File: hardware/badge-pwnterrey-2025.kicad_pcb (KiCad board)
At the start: 2 copper layers, 47 x 50 mm, 0 parts

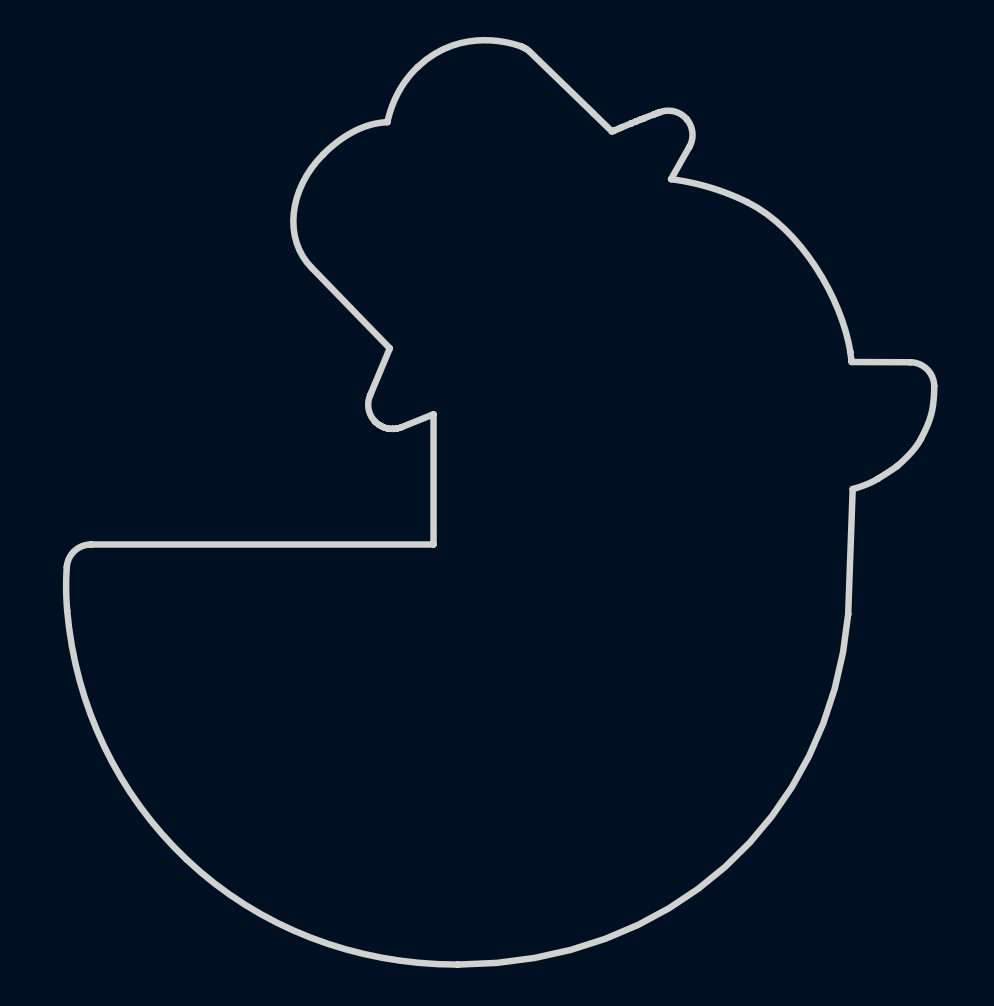
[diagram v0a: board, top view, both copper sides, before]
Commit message: feat(hw): add floorplan
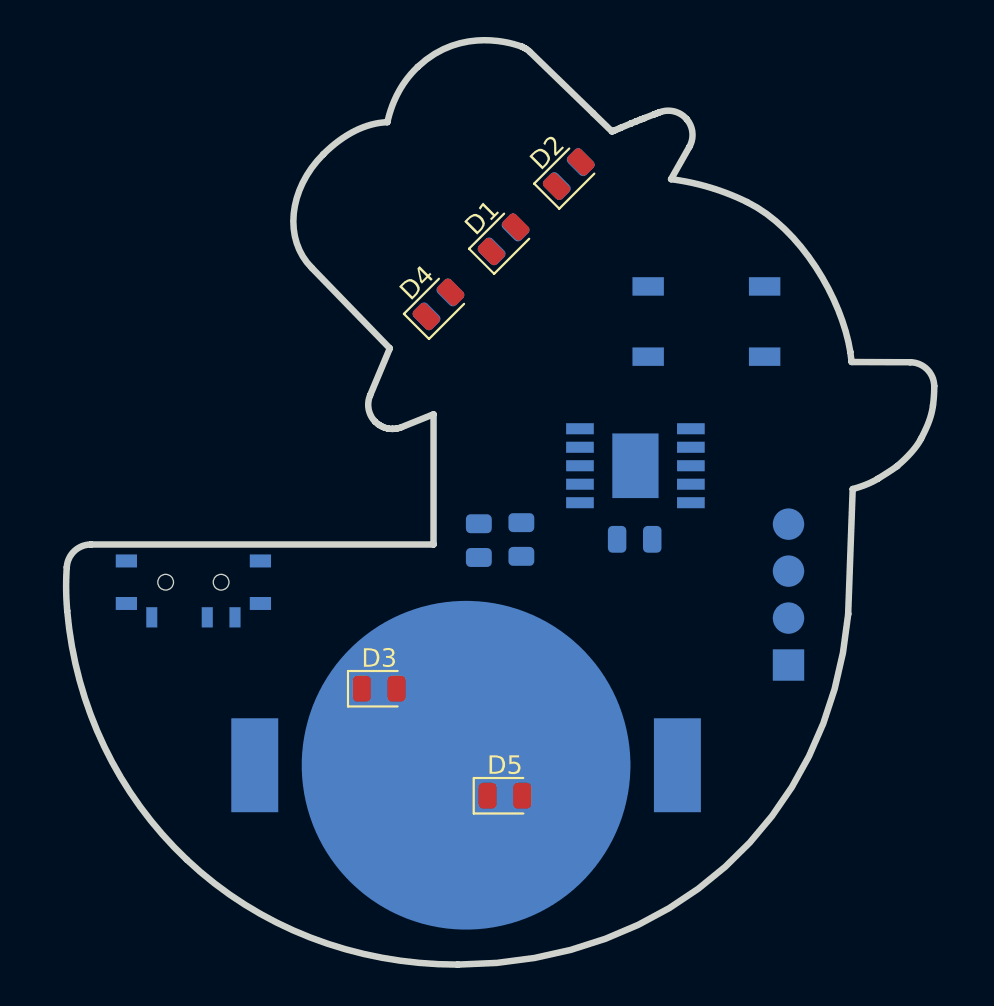
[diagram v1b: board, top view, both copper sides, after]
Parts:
- added BT1: Battery_Cell, Library:BAT-HLD-001, B.Cu at (145.0, 113.0)
- added C1: 0.1uF, Capacitor_SMD:C_0805_2012Metric, B.Cu at (154.1, 100.8)
- added D1: Orange, LED_SMD:LED_0805_2012Metric, F.Cu at (147.0, 84.5)
- added D2: Red, LED_SMD:LED_0805_2012Metric, F.Cu at (150.6, 81.0)
- added D3: Blue, LED_SMD:LED_0805_2012Metric, F.Cu at (140.3, 108.9)
- added D4: Green, LED_SMD:LED_0805_2012Metric, F.Cu at (143.5, 88.1)
- added D5: Yellow, LED_SMD:LED_0805_2012Metric, F.Cu at (147.1, 114.7)
- added J1: Conn_01x04_Socket, Connector_PinHeader_2.54mm:PinHeader_1x04_P2.54mm_Vertical, B.Cu at (162.4, 107.6)
- added R1: 330R, Resistor_SMD:R_0805_2012Metric, B.Cu at (147.0, 84.6)
- added R2: 330R, Resistor_SMD:R_0805_2012Metric, B.Cu at (150.6, 81.0)
- added R3: 330R, Resistor_SMD:R_0805_2012Metric, B.Cu at (145.7, 100.8)
- added R4: 330R, Resistor_SMD:R_0805_2012Metric, B.Cu at (143.5, 88.1)
- added R5: 330R, Resistor_SMD:R_0805_2012Metric, B.Cu at (148.0, 100.8)
- added SW1: SW_RST, Button_Switch_SMD:SW_SPST_TL3342, B.Cu at (158.0, 89.0)
- added SW2: On, Library:MSK12C02, B.Cu at (130.2, 103.1)
- added U1: PY32F002AA15M6TU, Library:PY32F002AA15M, B.Cu at (154.2, 96.8)

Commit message: feat(hw): add routes
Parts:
- moved R5 1.10 mm to (148.0, 99.7)
- moved R3 1.10 mm to (145.7, 99.8)
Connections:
- J1 pad 2: +3V3 -> +3.3V
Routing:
- net +3.3V: track 0.00 -> 57.5 mm, vias 0 -> 2
- net /PA7: track 0.00 -> 23.7 mm, vias 0 -> 1
- net Net-(D5-A): track 0.00 -> 22.1 mm, vias 0 -> 1
- net /NRST: track 0.00 -> 21.5 mm
- net /PA6: track 0.00 -> 19.1 mm, vias 0 -> 1
- net Net-(BT1--): track 0.00 -> 19.0 mm
- net /PA1: track 0.00 -> 13.3 mm, vias 0 -> 1
- net Net-(D3-A): track 0.00 -> 12.4 mm, vias 0 -> 1
- net /SWCLK: track 0.00 -> 9.35 mm
- net /SWDIO: track 0.00 -> 7.75 mm
- net /PA5: track 0.00 -> 6.96 mm
- net /PF0: track 0.00 -> 3.87 mm
- net Net-(D1-K): track 0.00 -> 2.54 mm, vias 0 -> 1
- net Net-(D2-K): track 0.00 -> 2.51 mm, vias 0 -> 1
- net Net-(D4-K): track 0.00 -> 2.19 mm, vias 0 -> 1
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- added copper zone on B.Cu, net GND
- added copper zone on F.Cu, net GND
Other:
- board size 47 x 50 mm -> 46.9 x 50 mm

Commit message: feat(Hw):Added_Labels
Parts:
- added G***: LOGO, Symbol_EC:electronic_cats_logo_8x6, B.Cu at (148.8, 90.2)
- added kibuzzard-67D45E5B: G***, kibuzzard-67D45E5B, B.Cu at (127.9, 107.6)
- added kibuzzard-67D45E75: G***, kibuzzard-67D45E75, B.Cu at (132.1, 107.7)
- added kibuzzard-67D45F14: G***, kibuzzard-67D45F14, B.Cu at (159.6, 105.1)
- added kibuzzard-67D45F29: G***, kibuzzard-67D45F29, B.Cu at (159.6, 107.8)
- added kibuzzard-67D45F47: G***, kibuzzard-67D45F47, B.Cu at (158.9, 102.5)
- added kibuzzard-67D45F59: G***, kibuzzard-67D45F59, B.Cu at (158.9, 100.0)
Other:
- board text added: "v1.0"

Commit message: feat(hw): move routes
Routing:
- net Net-(D5-A): track 22.1 -> 14.1 mm
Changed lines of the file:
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@@
 				(polygon
 					(pts
-						(xy 149.310337 90.191595) (xy 149.310337 90.12184) (xy 149.055787 90.121437) (xy 149.055787 90.344589)
-						(xy 149.096085 90.373662) (xy 149.13634 90.396931) (xy 149.176724 90.414821) (xy 149.218765 90.427946)
-						(xy 149.261288 90.435768) (xy 149.304585 90.438378) (xy 149.362669 90.434035) (xy 149.416031 90.421338)
-						(xy 149.465493 90.40046) (xy 149.499696 90.379201) (xy 149.529042 90.35401) (xy 149.553967 90.324689)
-						(xy 149.574706 90.290844) (xy 149.594984 90.241835) (xy 149.607356 90.188684) (xy 149.611599 90.130559)
-						(xy 149.607458 90.072936) (xy 149.595227 90.018574) (xy 149.574926 89.966831) (xy 149.554099 89.930582)
-						(xy 149.529667 89.900042) (xy 149.50153 89.874612) (xy 149.469376 89.853918) (xy 149.422186 89.833763)
-						(xy 149.36965 89.821333) (xy 149.31074 89.817025) (xy 149.267689 89.819472) (xy 149.228585 89.826559)
-						(xy 149.192918 89.838017) (xy 149.159414 89.854388) (xy 149.132167 89.873895) (xy 149.110339 89.896526)
-						(xy 149.092699 89.922762) (xy 149.077431 89.955017) (xy 149.0648 89.994308) (xy 149.136534 90.013982)
-						(xy 149.152523 89.971386) (xy 149.170166 89.942065) (xy 149.184916 89.92627) (xy 149.203813 89.912303)
-						(xy 149.227539 89.900189) (xy 149.266291 89.888488) (xy 149.310337 89.884436) (xy 149.34641 89.88644)
-						(xy 149.377604 89.892115) (xy 149.404603 89.901069) (xy 149.441182 89.920778) (xy 149.468753 89.944812)
-						(xy 149.490496 89.973352) (xy 149.506672 90.00431) (xy 149.519299 90.042159) (xy 149.526987 90.082395)
-						(xy 149.529606 90.12543) (xy 149.526218 90.178556) (xy 149.516745 90.222986) (xy 149.501946 90.260142)
-						(xy 149.480495 90.293425) (xy 149.453824 90.320013) (xy 149.421419 90.340596) (xy 149.385392 90.3552)
-						(xy 149.348094 90.363929) (xy 149.309092 90.366864) (xy 149.275051 90.364675) (xy 149.241542 90.358104)
-						(xy 149.208305 90.347044) (xy 149.162857 90.3253) (xy 149.133677 90.304729) (xy 149.133677 90.191595)
+						(xy 149.614053 90.138143) (xy 149.610615 90.08087) (xy 149.60088 90.031479) (xy 149.585488 89.988822)
+						(xy 149.564755 89.951929) (xy 149.538656 89.920046) (xy 149.507286 89.893128) (xy 149.471208 89.871878)
+						(xy 149.429731 89.856185) (xy 149.381934 89.846299) (xy 149.326714 89.842817) (xy 149.263339 89.846849)
+						(xy 149.212167 89.857944) (xy 149.171009 89.874983) (xy 149.143304 89.893066) (xy 149.118813 89.915899)
+						(xy 149.097306 89.943953) (xy 149.078759 89.977932) (xy 149.15335 89.999914) (xy 149.172279 89.969833)
+						(xy 149.19481 89.946483) (xy 149.221201 89.929022) (xy 149.250841 89.917104) (xy 149.286313 89.909477)
+						(xy 149.328765 89.906747) (xy 149.378226 89.910962) (xy 149.419187 89.922791) (xy 149.453272 89.941565)
+						(xy 149.481649 89.967381) (xy 149.503718 89.998851) (xy 149.520188 90.036875) (xy 149.530734 90.082762)
+						(xy 149.534516 90.138143) (xy 149.530585 90.192977) (xy 149.519526 90.239205) (xy 149.502062 90.278282)
+						(xy 149.478389 90.31136) (xy 149.448262 90.338675) (xy 149.413065 90.358315) (xy 149.371791 90.370541)
+						(xy 149.323014 90.374851) (xy 149.267825 90.370447) (xy 149.217501 90.357595) (xy 149.185897 90.344181)
+						(xy 149.159694 90.328501) (xy 149.138183 90.310664) (xy 149.138183 90.206177) (xy 149.31074 90.206177)
+						(xy 149.31074 90.140598) (xy 149.066046 90.140598) (xy 149.066046 90.340229) (xy 149.09852 90.368771)
+						(xy 149.135835 90.392923) (xy 149.178556 90.412733) (xy 149.223604 90.426832) (xy 149.271615 90.43544)
+						(xy 149.32305 90.438378) (xy 149.382527 90.434085) (xy 149.434151 90.421846) (xy 149.479195 90.402255)
+						(xy 149.510109 90.382144) (xy 149.536928 90.358265) (xy 149.559982 90.330393) (xy 149.579432 90.298134)
+						(xy 149.598213 90.251613) (xy 149.609945 90.198673)
 					)
 				)
 				(polygon
 					(pts
-						(xy 148.977019 89.938951) (xy 148.958151 89.880332) (xy 148.897804 89.902817) (xy 148.863483 89.918947)
-						(xy 148.871689 89.817025) (xy 148.812265 89.817025) (xy 148.814983 89.860038) (xy 148.821681 89.918544)
-						(xy 148.777658 89.899141) (xy 148.724961 89.880332) (xy 148.706093 89.938951) (xy 148.758142 89.952428)
-						(xy 148.808162 89.960346) (xy 148.781331 89.986953) (xy 148.737637 90.037759) (xy 148.786839 90.0726)
-						(xy 148.811131 90.036968) (xy 148.843003 89.984526) (xy 148.873294 90.038402) (xy 148.896272 90.0726)
-						(xy 148.944633 90.037759) (xy 148.899857 89.984608) (xy 148.876599 89.960346)
+						(xy 148.816332 89.973426) (xy 148.708144 89.931074) (xy 148.689716 89.985332) (xy 148.805268 90.015338)
+						(xy 148.729467 90.11803) (xy 148.77823 90.147632) (xy 148.839706 90.041606) (xy 148.903636 90.146826)
+						(xy 148.952436 90.117224) (xy 148.87495 90.015338) (xy 148.989732 89.985332) (xy 148.971267 89.930268)
+						(xy 148.861834 89.974232) (xy 148.86678 89.852196) (xy 148.811019 89.852196)
 					)
 				)
 				(polygon
 					(pts
-						(xy 148.650515 89.938951) (xy 148.631648 89.880332) (xy 148.5713 89.902817) (xy 148.536979 89.918947)
-						(xy 148.545186 89.817025) (xy 148.485761 89.817025) (xy 148.48848 89.860038) (xy 148.495177 89.918544)
-						(xy 148.451155 89.899141) (xy 148.398457 89.880332) (xy 148.379589 89.938951) (xy 148.431638 89.952428)
-						(xy 148.481658 89.960346) (xy 148.454828 89.986953) (xy 148.411133 90.037759) (xy 148.460336 90.0726)
-						(xy 148.484627 90.036968) (xy 148.516499 89.984526) (xy 148.546791 90.038402) (xy 148.569769 90.0726)
-						(xy 148.618129 90.037759) (xy 148.573354 89.984608) (xy 148.550095 89.960346)
+						(xy 148.489828 89.973426) (xy 148.381641 89.931074) (xy 148.363212 89.985332) (xy 148.478764 90.015338)
+						(xy 148.402963 90.11803) (xy 148.451726 90.147632) (xy 148.513202 90.041606) (xy 148.577133 90.146826)
+						(xy 148.625932 90.117224) (xy 148.548446 90.015338) (xy 148.663228 89.985332) (xy 148.644763 89.930268)
+						(xy 148.53533 89.974232) (xy 148.540276 89.852196) (xy 148.484516 89.852196)
 					)
 				)
 				(polygon
 					(pts
-						(xy 148.324011 89.938951) (xy 148.305144 89.880332) (xy 148.244796 89.902817) (xy 148.210475 89.918947)
-						(xy 148.218682 89.817025) (xy 148.159257 89.817025) (xy 148.161976 89.860038) (xy 148.168673 89.918544)
-						(xy 148.124651 89.899141) (xy 148.071953 89.880332) (xy 148.053085 89.938951) (xy 148.105134 89.952428)
-						(xy 148.155154 89.960346) (xy 148.128324 89.986953) (xy 148.084629 90.037759) (xy 148.133832 90.0726)
-						(xy 148.158123 90.036968) (xy 148.189995 89.984526) (xy 148.220287 90.038402) (xy 148.243265 90.0726)
-						(xy 148.291625 90.037759) (xy 148.24685 89.984608) (xy 148.223591 89.960346)
+						(xy 148.163324 89.973426) (xy 148.055137 89.931074) (xy 148.036709 89.985332) (xy 148.15226 90.015338)
+						(xy 148.076459 90.11803) (xy 148.125222 90.147632) (xy 148.186698 90.041606) (xy 148.250629 90.146826)
+						(xy 148.299428 90.117224) (xy 148.221942 90.015338) (xy 148.336724 89.985332) (xy 148.31826 89.930268)
+						(xy 148.208827 89.974232) (xy 148.213772 89.852196) (xy 148.158012 89.852196)
 					)
 				)
@@
 	)
 	(segment
-		(start 141.285 102.655)
-		(end 140.69 103.25)
-		(width 0.4)
-		(layer "F.Cu")
-		(net 9)
-	)
-	(segment
-		(start 141.237501 108.007501)
+		(start 145.24 108.86)
 		(end 141.237501 108.86)
-		(width 0.4)
+		(width 0.3)
 		(layer "F.Cu")
 		(net 9)
 	)
 	(segment
-		(start 140.69 107.46)
-		(end 141.237501 108.007501)
-		(width 0.4)
+		(start 145.7 108.4)
+		(end 145.24 108.86)
+		(width 0.3)
 		(layer "F.Cu")
 		(net 9)
 	)
 	(segment
-		(start 140.69 103.25)
-		(end 140.69 107.46)
-		(width 0.4)
+		(start 145.7 102.8)
+		(end 145.7 108.4)
+		(width 0.3)
 		(layer "F.Cu")
 		(net 9)
 	)
 	(via
-		(at 141.285 102.655)
+		(at 145.7 102.8)
 		(size 0.6)
 		(drill 0.3)
@@
 	)
 	(segment
-		(start 141.285 102.655)
-		(end 141.81 102.13)
-		(width 0.4)
-		(layer "B.Cu")
-		(net 9)
-	)
-	(segment
-		(start 145.68 101.45)
-		(end 145.68 100.6625)
-		(width 0.4)
-		(layer "B.Cu")
-		(net 9)
-	)
-	(segment
-		(start 141.81 102.13)
-		(end 145 102.13)
-		(width 0.4)
+		(start 145.68 100.6625)
+		(end 145.68 102.78)
+		(width 0.3)
 		(layer "B.Cu")
 		(net 9)
 	)
 	(segment
-		(start 145 102.13)
-		(end 145.68 101.45)
-		(width 0.4)
+		(start 145.68 102.78)
+		(end 145.7 102.8)
+		(width 0.3)
 		(layer "B.Cu")
 		(net 9)
@@
 	)
 	(segment
-		(start 141.84 106.45)
-		(end 148.037501 112.647501)
-		(width 0.4)
-		(layer "F.Cu")
-		(net 13)
-	)
-	(segment
-		(start 141.832913 103.83)
-		(end 141.832913 104.16022)
-		(width 0.4)
-		(layer "F.Cu")
-		(net 13)
-	)
-	(segment
-		(start 141.832913 104.16022)
-		(end 141.84 104.167307)
-		(width 0.4)
-		(layer "F.Cu")
-		(net 13)
-	)
-	(segment
-		(start 141.84 104.167307)
-		(end 141.84 106.45)
-		(width 0.4)
+		(start 148.037501 102.837501)
+		(end 148.037501 114.65)
+		(width 0.3)
 		(layer "F.Cu")
 		(net 13)
 	)
 	(segment
-		(start 148.037501 112.647501)
-		(end 148.037501 114.65)
-		(width 0.4)
+		(start 148 102.8)
+		(end 148.037501 102.837501)
+		(width 0.3)
 		(layer "F.Cu")
 		(net 13)
 	)
 	(via
-		(at 141.832913 103.83)
+		(at 148 102.8)
 		(size 0.6)
 		(drill 0.3)
@@
 	)
 	(segment
-		(start 147.38 102.95)
-		(end 147.98 102.35)
-		(width 0.4)
-		(layer "B.Cu")
-		(net 13)
-	)
-	(segment
-		(start 142.41 102.95)
-		(end 147.38 102.95)
-		(width 0.4)
-		(layer "B.Cu")
-		(net 13)
-	)
-	(segment
-		(start 147.98 102.35)
-		(end 147.98 100.6025)
-		(width 0.4)
-		(layer "B.Cu")
-		(net 13)
-	)
-	(segment
-		(start 141.832913 103.527087)
-		(end 142.41 102.95)
-		(width 0.4)
+		(start 147.98 102.78)
+		(end 148 102.8)
+		(width 0.3)
 		(layer "B.Cu")
 		(net 13)
 	)
 	(segment
-		(start 141.832913 103.83)
-		(end 141.832913 103.527087)
-		(width 0.4)
+		(start 147.98 100.6025)
+		(end 147.98 102.78)
+		(width 0.3)
 		(layer "B.Cu")
 		(net 13)
